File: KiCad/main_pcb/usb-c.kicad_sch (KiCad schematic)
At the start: 15 parts, among them J6 USB_C_Receptacle_USB2.0_14P, J7 Conn_01x01, J8 Conn_01x01, U5 CH340C, U6 AMS1117-3.3

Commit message: feat(KiCad): Adds part reference and fetches version that was taken into account by 42Chips when ordering so I can fix errors on the matching production files for the current PCB. :)
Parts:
- added D5: LED, LED_SMD:LED_0603_1608Metric_Pad1.05x0.95mm_HandSolder, symbol Device:LED
- added R9: 330Ω, Resistor_SMD:R_0603_1608Metric_Pad0.98x0.95mm_HandSolder, symbol Device:R
- C14, C15, C16, C17, C18, C19: LCSC (none) -> C14663
- C20, C21: LCSC (none) -> C2762594
- J6: LCSC (none) -> C165948
- R7, R8: LCSC (none) -> C2907044
- U5: LCSC (none) -> C84681
- U6: LCSC (none) -> C5205141
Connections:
- net GND: now also R9.2
- net VCC: now also D5.2 (A)
- new net: D5.1 (K), R9.1
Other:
- moved on the sheet: J7

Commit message: feat(schematic): Fixing mistakes
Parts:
- C16: value 100nF -> 10uF
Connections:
- net RXD: now also U5.2 (TXD); no longer U5.3 (RXD)
- net TXD: now also U5.3 (RXD); no longer U5.2 (TXD)
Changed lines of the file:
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@@
 	(hierarchical_label "RXD"
 		(shape input)
-		(at 168.91 118.11 0)
+		(at 168.91 115.57 0)
 		(effects
 			(font
@@
 	(hierarchical_label "TXD"
 		(shape output)
-		(at 168.91 115.57 0)
+		(at 168.91 118.11 0)
 		(effects
 			(font
@@
 			)
 		)
-		(property "Value" "100nF"
+		(property "Value" "10uF"
 			(at 162.306 60.96 0)
 			(effects

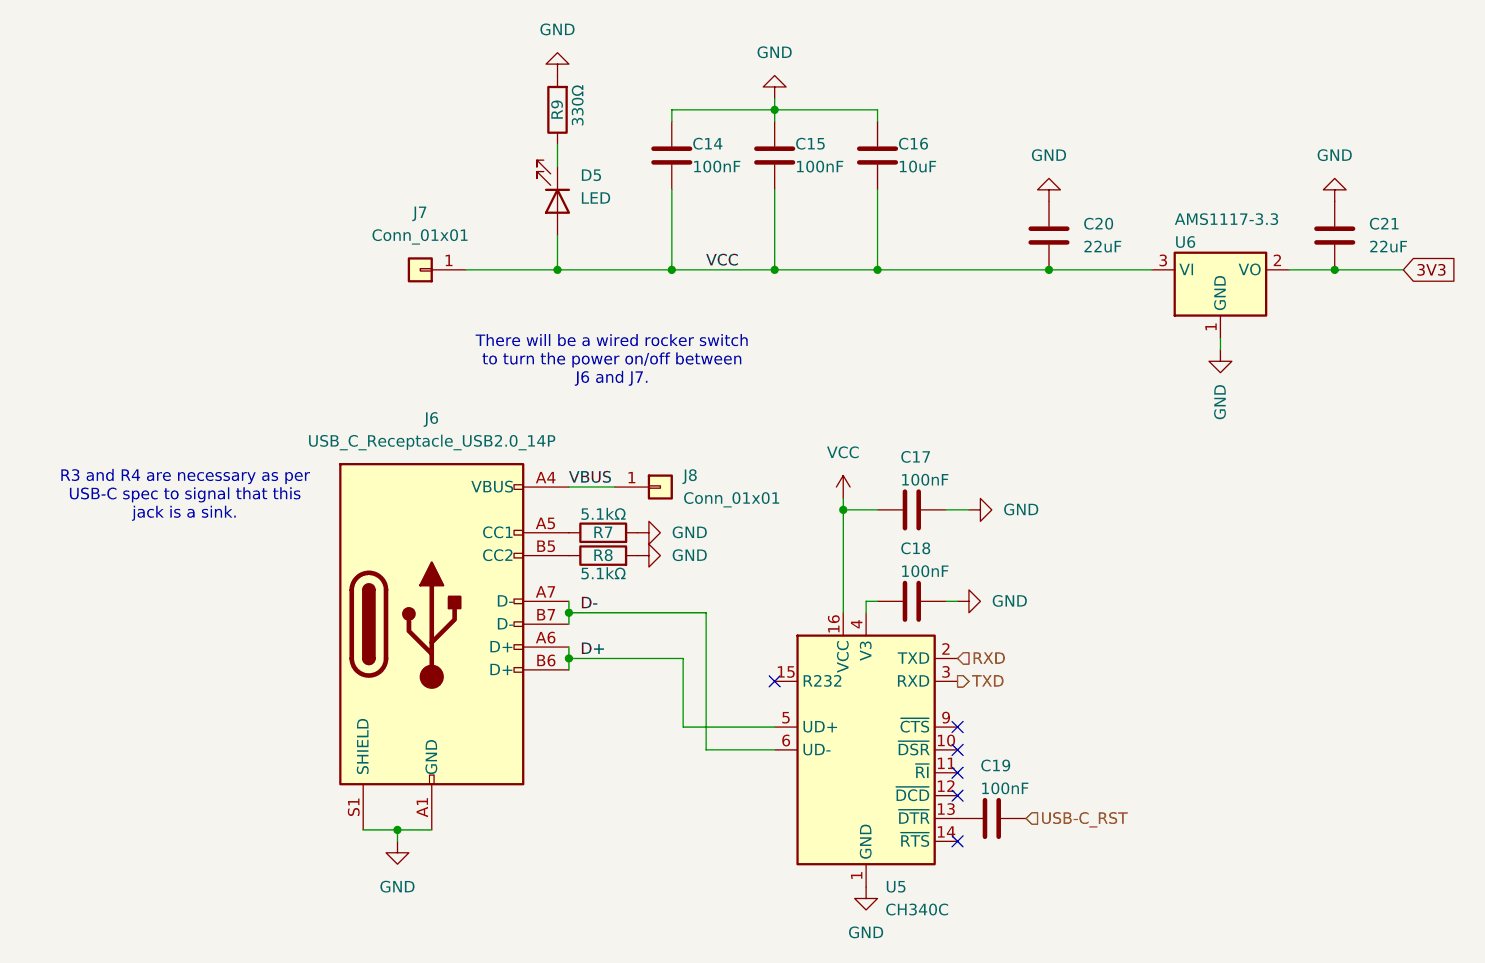
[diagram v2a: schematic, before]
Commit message: Main PCB v2 (#51)
* feat(schematic & pcb): Switches to 2 rows header for keyboard connection

* feat(pcb): Keeps working on version 2 of main PCB

* feat(PCB): Continues work on PCB v2.

* feat(PCB): Continues work

* feat(PCB): Continues work

* feat(pcb): Workinonit

* feat(footprints): Adds homebrew USB-C

* chore(migration): Migrates to homebrew symbols for PCB.

* feat(footprints): Reworking footprints to allow hand-soldering

* feat(pcb): I think that's about right

* feat(pcb): Should be a-ok

* feat(PCB): Adds two pins header for LED Backlight

* feat(pcb): Uses new footprint for Male Header 2x13

* feat(3D models): Adds 3D models to PCB

* feat(schematic): Changes LED's resistor values from 330 ohms to 1k ohms.

* feat(3D models): Adds 3D model for push button switch

* feat(pcb): Adds all the remaning 3D models

* chore: Adds 3D models to footprint, instead of adding manually when placing components :3

* chore

* feat(sourcing): Changes Main PCB <-> Keyboard PCB connectors to something in stock

* chore

* chore

* chore

---------

Co-authored-by: Madeline Wolff <git@firmaments.anonaddy.com>
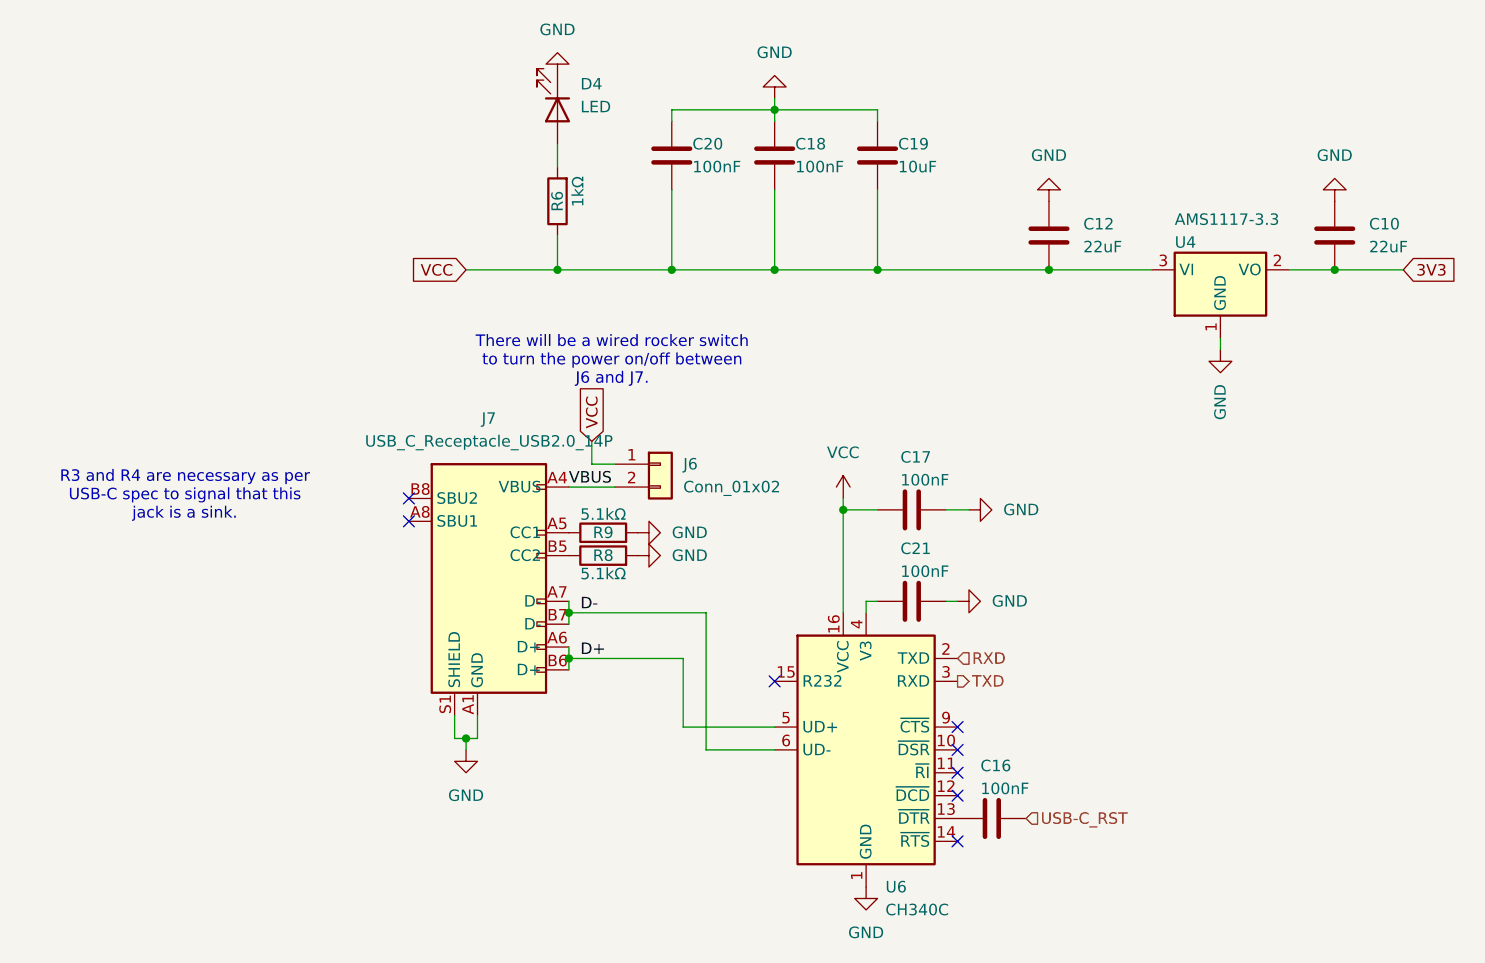
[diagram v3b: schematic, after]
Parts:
- removed J7, J8: Conn_01x01, Connector_PinHeader_2.54mm:PinHeader_1x01_P2.54mm_Vertical, symbol Connector_Generic:Conn_01x01
- added J6: Conn_01x02, Lilibrary:JST XH 2 pins, symbol Connector_Generic:Conn_01x02
- C10: renamed from C21; footprint Capacitor_SMD:C_0603_1608Metric_Pad1.08x0.95mm_HandSolder -> Lilibrary:Capacitor_0603
- C12: renamed from C20; footprint Capacitor_SMD:C_0603_1608Metric_Pad1.08x0.95mm_HandSolder -> Lilibrary:Capacitor_0603
- C16: renamed from C19; footprint Capacitor_SMD:C_0603_1608Metric_Pad1.08x0.95mm_HandSolder -> Lilibrary:Capacitor_0603
- C17: footprint Capacitor_SMD:C_0603_1608Metric_Pad1.08x0.95mm_HandSolder -> Lilibrary:Capacitor_0603
- C18: renamed from C15; footprint Capacitor_SMD:C_0603_1608Metric_Pad1.08x0.95mm_HandSolder -> Lilibrary:Capacitor_0603
- C19: renamed from C16; footprint Capacitor_SMD:C_0603_1608Metric_Pad1.08x0.95mm_HandSolder -> Lilibrary:Capacitor_0603; LCSC C14663 -> C1691
- C20: renamed from C14; footprint Capacitor_SMD:C_0603_1608Metric_Pad1.08x0.95mm_HandSolder -> Lilibrary:Capacitor_0603
- C21: renamed from C18; footprint Capacitor_SMD:C_0603_1608Metric_Pad1.08x0.95mm_HandSolder -> Lilibrary:Capacitor_0603
- D4: renamed from D5; footprint LED_SMD:LED_0603_1608Metric_Pad1.05x0.95mm_HandSolder -> Lilibrary:LED_0603
- J7: renamed from J6; footprint Connector_USB:USB_C_Receptacle_HRO_TYPE-C-31-M-12 -> Lilibrary:USB_C_Receptacle_HRO_TYPE-C-31-M-12; symbol Connector:USB_C_Receptacle_USB2.0_14P -> Lilybrary:USB-C
- R6: renamed from R9; value 330Ω -> 1kΩ; footprint Resistor_SMD:R_0603_1608Metric_Pad0.98x0.95mm_HandSolder -> Lilibrary:Resistor_0603; LCSC C2933198 -> C22548
- R8: footprint Resistor_SMD:R_0603_1608Metric_Pad0.98x0.95mm_HandSolder -> Lilibrary:Resistor_0603
- R9: renamed from R7; footprint Resistor_SMD:R_0603_1608Metric_Pad0.98x0.95mm_HandSolder -> Lilibrary:Resistor_0603
- renumbered U6 to U4, U5 to U6
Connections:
- net GND: now also D4.1 (K); no longer R6.2
- net VBUS: now also J6.2 (Pin_2)
- net VCC: now also R6.1, J6.1 (Pin_1); no longer D4.2 (A)
- new net: D4.2 (A), R6.2
- no-connect marks 6 -> 8
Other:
- moved on the sheet: D4, R6
